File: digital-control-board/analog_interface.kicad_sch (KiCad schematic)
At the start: 38 parts, among them U5 DAC8551IADGKR, U6 ADS131M04IPWR, U7 ADS131M02IPWR, X1 SG-8018CE-8.192000MHZ-TJHSA

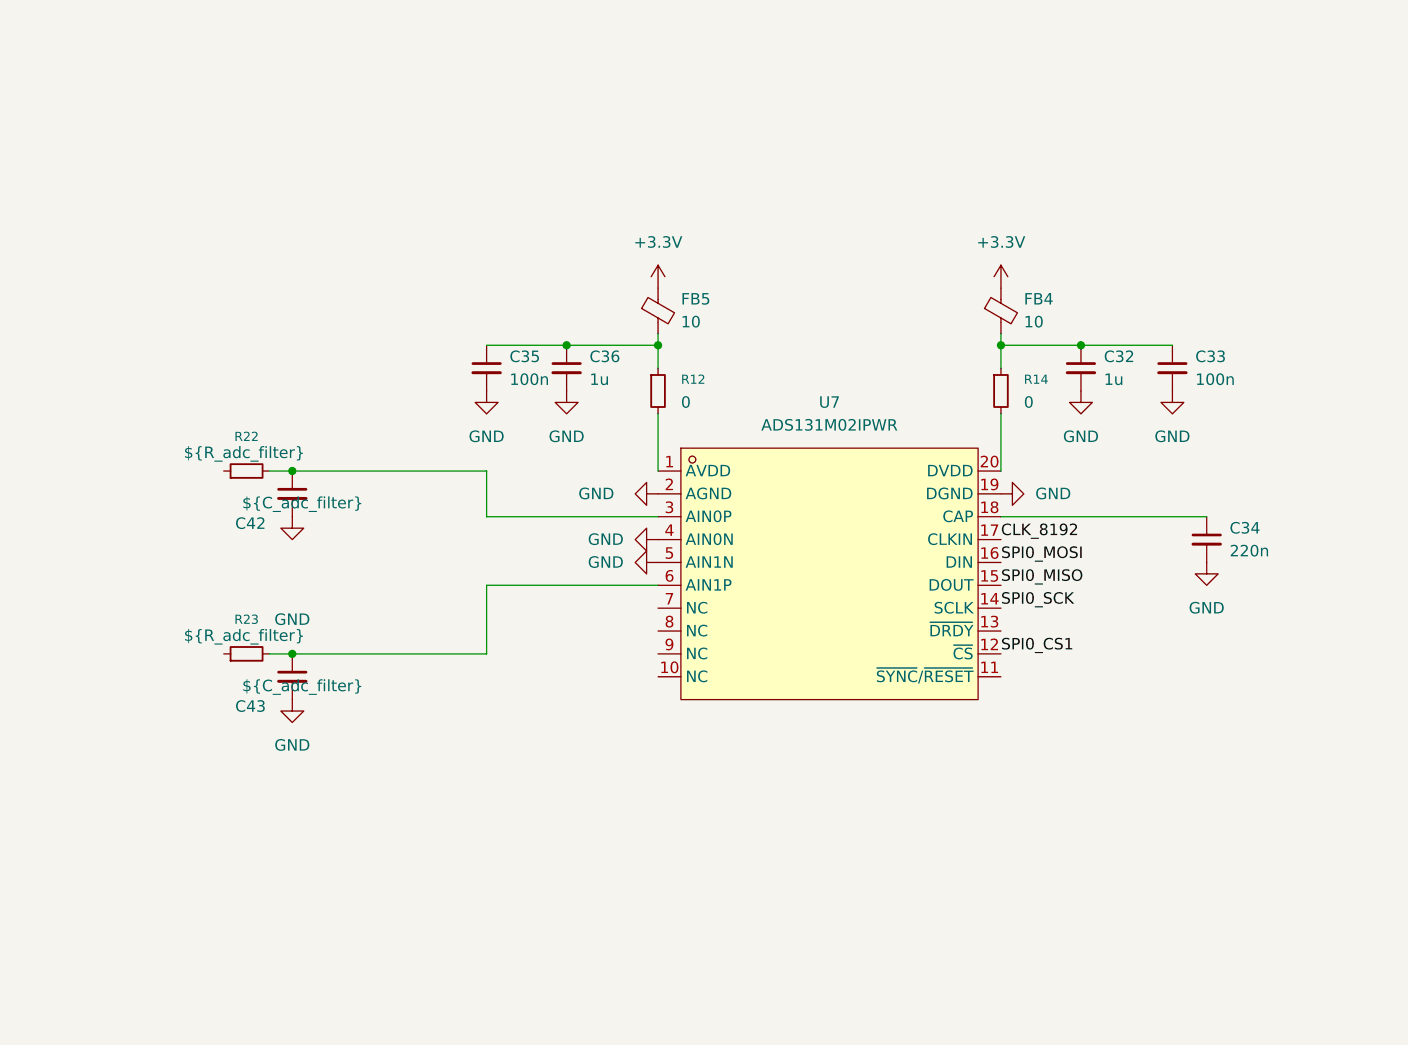
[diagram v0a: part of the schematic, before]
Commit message: Rearrange design in load control board, need further check
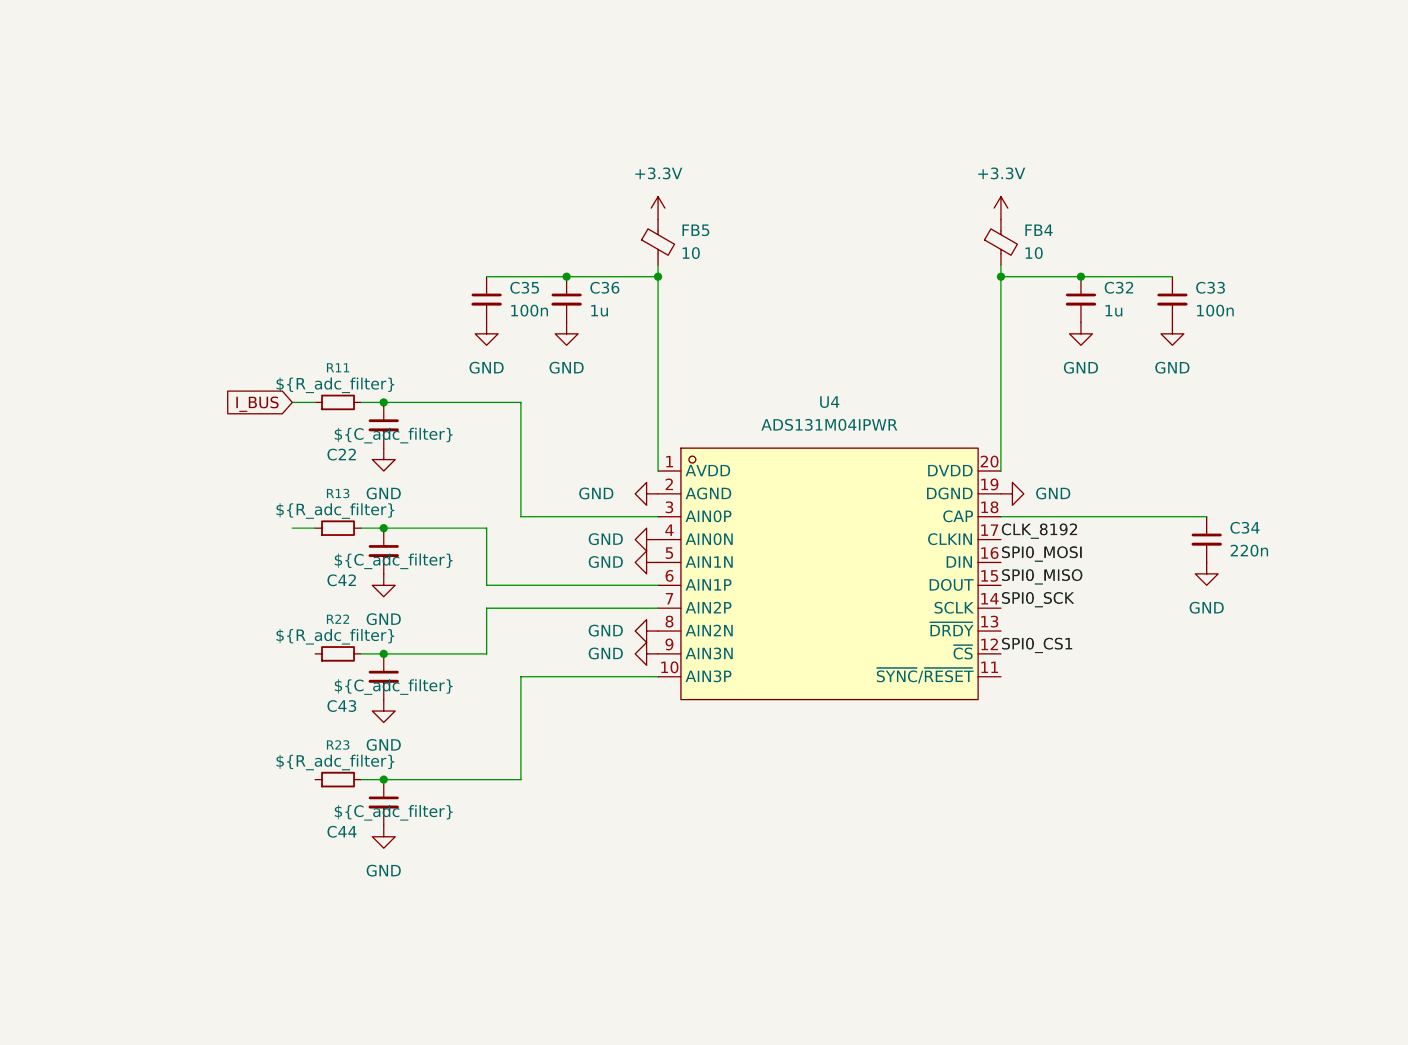
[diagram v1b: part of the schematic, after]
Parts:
- removed R12, R14: 0, Resistor_SMD:R_0603_1608Metric, symbol Device:R_Small
- removed U7: ADS131M02IPWR, programmable-load-library:TSSOP-20_L6.5-W4.4-P0.65-LS6.4-BL, symbol programmable-load-library:ADS131M02IPWR
- added C22, C44: ${C_adc_filter}, symbol Device:C_Small
- added R11, R13: ${R_adc_filter}, symbol Device:R_Small
- added U4: ADS131M04IPWR, programmable-load-library:TSSOP-20_L6.5-W4.4-P0.65-LS6.4-BL, symbol programmable-load-library:ADS131M04IPWR
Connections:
- net CLK_8192: now also U4.17 (CLKIN)
- net GND: now also C22.2, C44.2, U4.19 (DGND), U4.2 (AGND), U4.4 (AIN0N), U4.5 (AIN1N), U4.8 (AIN2N), U4.9 (AIN3N)
- net GPIO1: now also U4.12 (~{CS})
- net GPIO4: now also U4.15 (DOUT)
- net GPIO6: now also U4.14 (SCLK)
- net GPIO7: now also U4.16 (DIN)
- net at C32.1, C33.1, FB4.2: now also U4.20 (DVDD)
- net at C42.1: now also R13.2, U4.6 (AIN1P); no longer R22.2
- net at C35.1, C36.1, FB5.2: now also U4.1 (AVDD)
- net at C43.1: now also R22.2, U4.7 (AIN2P); no longer R23.2
- net at C34.1: now also U4.18 (CAP)
- new net: C22.1, R11.2, U4.3 (AIN0P)
- new net: C44.1, R23.2, U4.10 (AIN3P)
- new net I_BUS: R11.1
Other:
- moved on the sheet: C32, C33, C35, C36, FB4, FB5
